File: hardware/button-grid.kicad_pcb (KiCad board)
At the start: 2 copper layers, 208 x 110 mm, 108 parts, among them J1 12V DC, J11 LEDs, J12 LEDs, J13 LEDs, J14 LEDs, J15 LEDs, J16 LEDs, J17 LEDs, J18 LEDs, J2 USB-C, J3 ROWS, J4 COLS, J5 UART, SW1 RESET, SW2 BOOT, U1 ESP32-S3-WROOM-1-N8, U11 74HC595, U12 74HC595, U13 74HC595, U14 74HC595, U15 74HC595, U16 74HC595, U17 74HC595, U18 74HC595, U2 TPS54202H, U21 ULN2803A, U22 ULN2803A, U23 ULN2803A, U24 ULN2803A, U25 ULN2803A, U26 ULN2803A, U27 ULN2803A, U28 ULN2803A

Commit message: Regenerate project with deterministic UUIDs; route without optimizer; zoom renders
Co-Authored-By: Claude Opus 5.5 <noreply@anthropic.com>
Claude-Session: https://claude.ai/code/session_01USgdVYHDQPVjqMcbCmVwPa
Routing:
- net VBUS: track 0.00 -> 8.40 mm, vias 0 -> 2

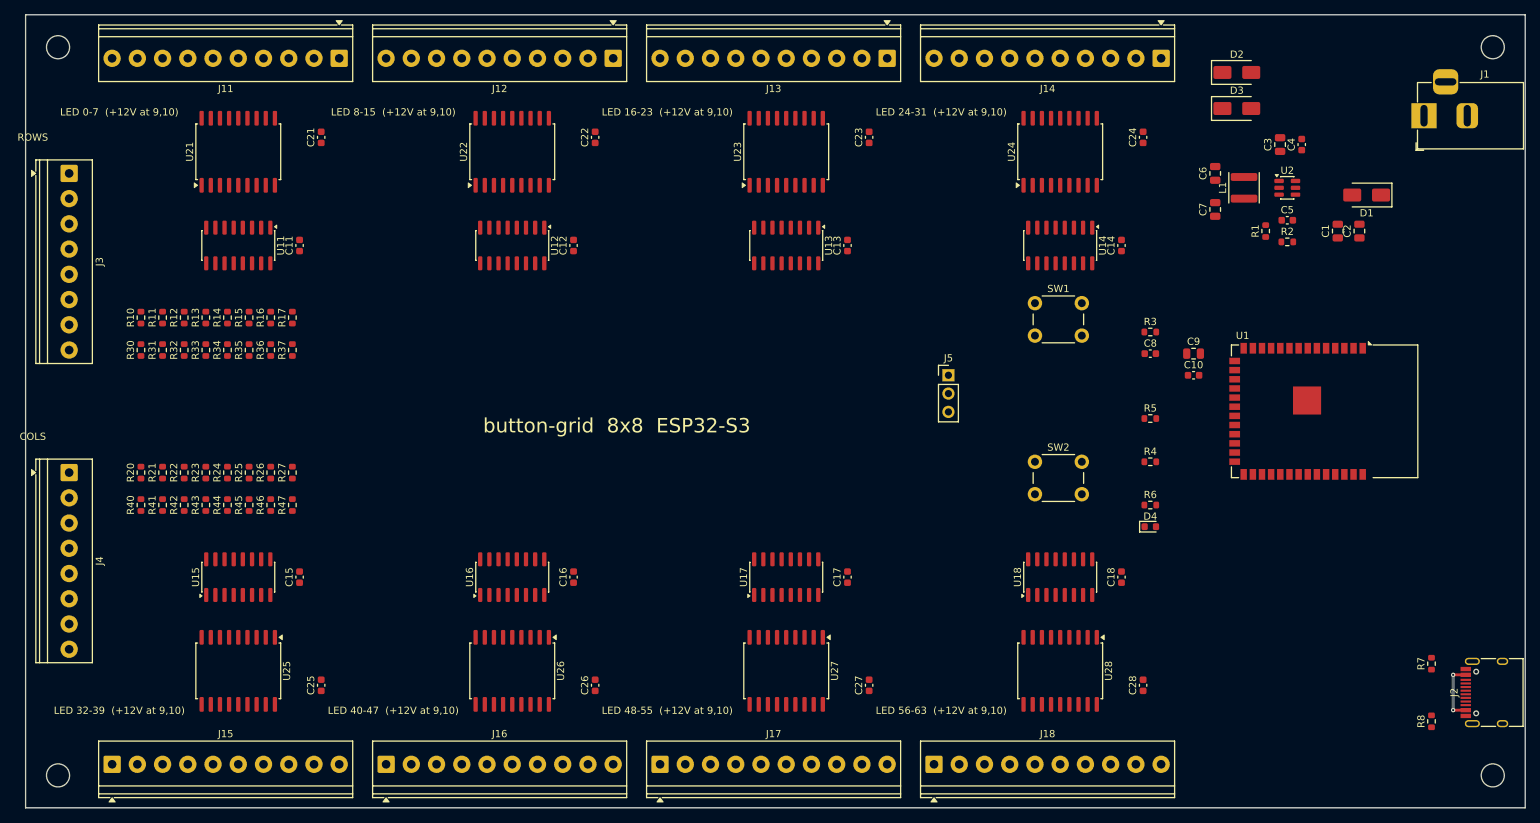
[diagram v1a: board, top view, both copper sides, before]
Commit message: Fully routed board: 0 DRC errors, ERC/netlist checks pass
- autorouted with Freerouting (10um clearance margin), locked USB VBUS bridge
- GND pours both sides, stitching vias, solid GND on THT pins
- run checks on every branch; Pages deploy from main

Co-Authored-By: Claude Opus 5.5 <noreply@anthropic.com>
Claude-Session: https://claude.ai/code/session_01USgdVYHDQPVjqMcbCmVwPa
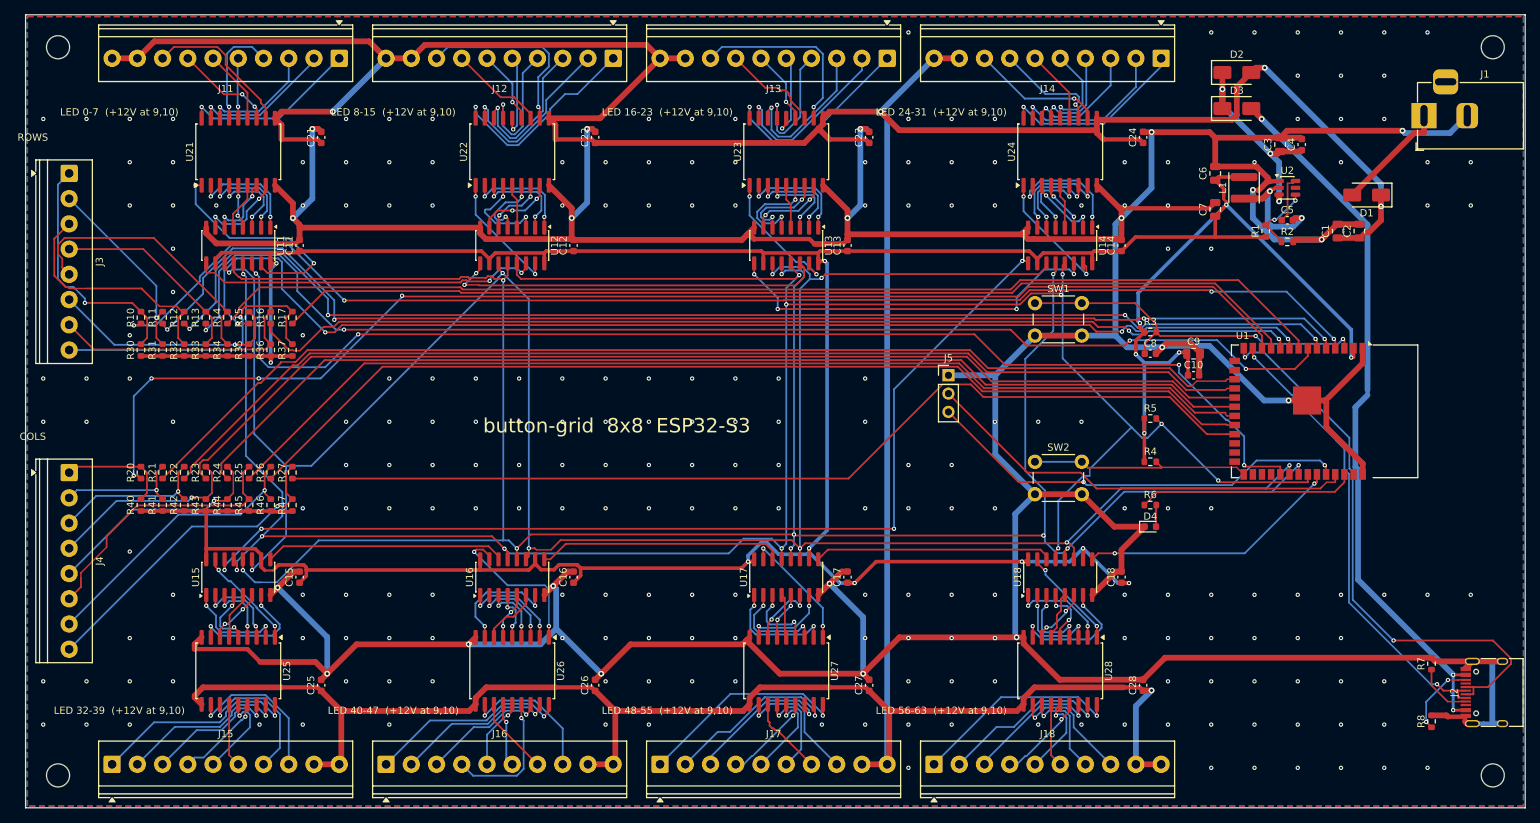
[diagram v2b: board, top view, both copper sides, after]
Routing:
- net GND: track 0.00 -> 788.8 mm, vias 0 -> 252
- net +12V: track 0.00 -> 591.0 mm, vias 0 -> 5
- net +3V3: track 0.00 -> 516.8 mm, vias 0 -> 15
- net /SRCLK: track 0.00 -> 332.8 mm, vias 0 -> 9
- net /OE_N: track 0.00 -> 329.4 mm, vias 0 -> 12
- net /RCLK: track 0.00 -> 327.5 mm, vias 0 -> 10
- net /ROW0: track 0.00 -> 180.5 mm, vias 0 -> 4
- net /COL0: track 0.00 -> 179.7 mm, vias 0 -> 4
- net /ROW1: track 0.00 -> 176.0 mm, vias 0 -> 4
- net /ROW2: track 0.00 -> 172.4 mm, vias 0 -> 4
- net /ROW3: track 0.00 -> 172.3 mm, vias 0 -> 4
- net /SER0: track 0.00 -> 169.2 mm, vias 0 -> 4
- net /ROW5: track 0.00 -> 168.0 mm, vias 0 -> 4
- net /COL1: track 0.00 -> 158.6 mm
- net /ROW4: track 0.00 -> 156.2 mm
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- added copper zone on B.Cu, net GND
- added copper zone on F.Cu, net GND
